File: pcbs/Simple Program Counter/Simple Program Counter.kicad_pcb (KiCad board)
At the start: 2 copper layers, 18 parts, among them U201 74HCT574, U202 74HC245, U203 74HC14

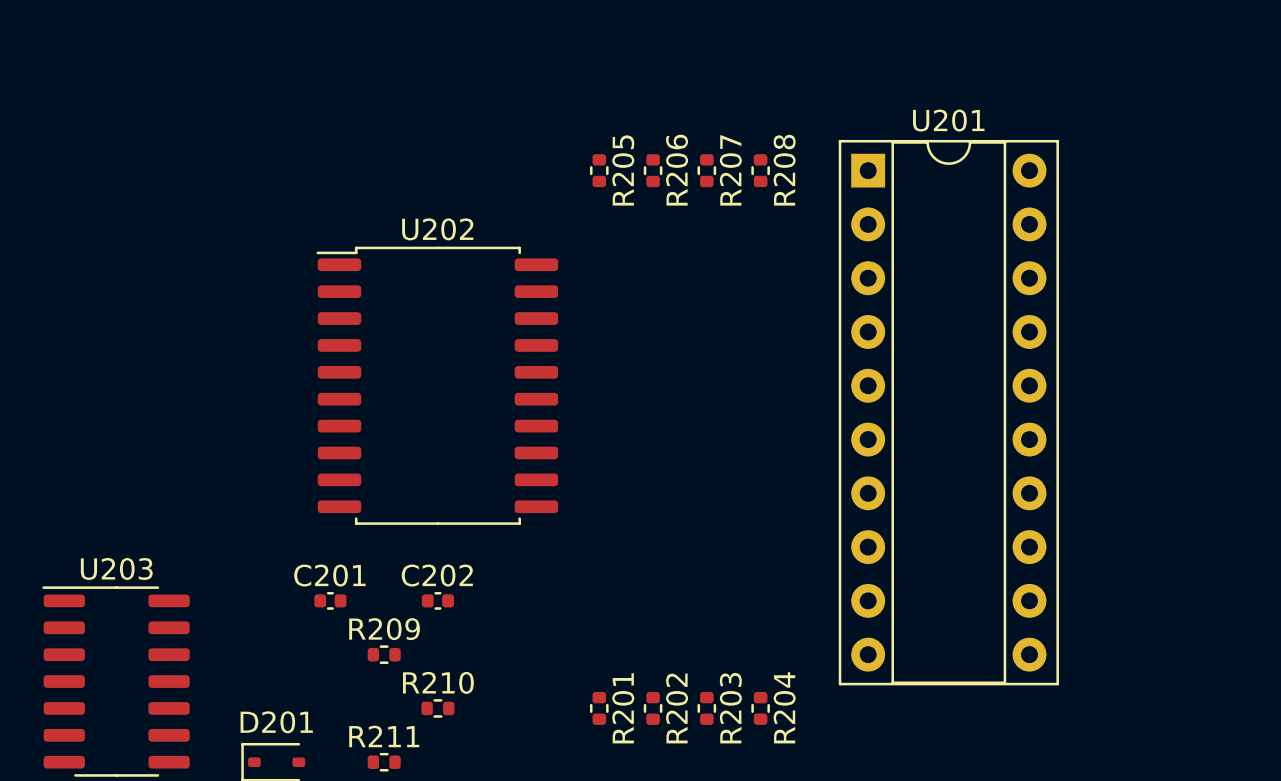
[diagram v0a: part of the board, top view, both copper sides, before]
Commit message: Adding indicator LEDs
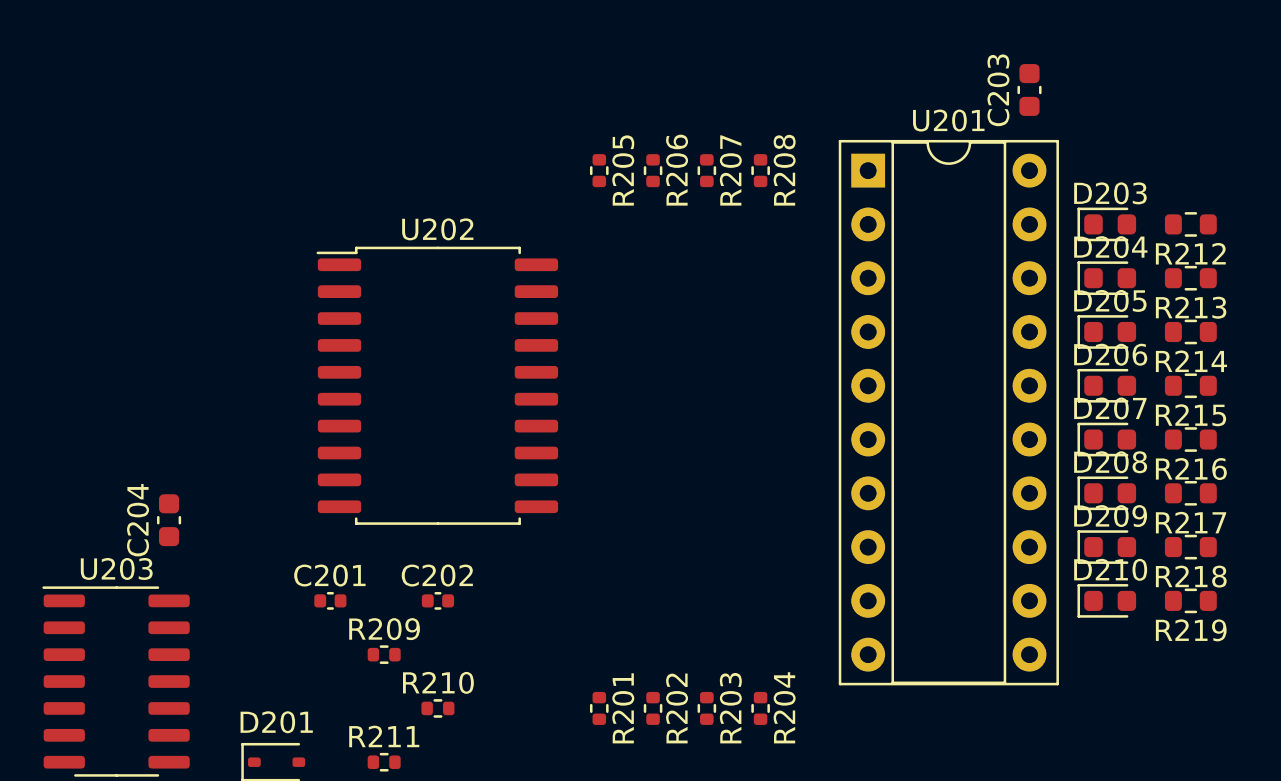
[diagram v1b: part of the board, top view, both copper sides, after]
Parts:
- added C203: 100n, Capacitor_SMD:C_0603_1608Metric, F.Cu at (139.7, 97.8)
- added C204: 100n, Capacitor_SMD:C_0603_1608Metric, F.Cu at (99.1, 118.1)
- added D203: GREEN, LED_SMD:LED_0603_1608Metric, F.Cu at (143.5, 104.1)
- added D204: GREEN, LED_SMD:LED_0603_1608Metric, F.Cu at (143.5, 106.7)
- added D205: GREEN, LED_SMD:LED_0603_1608Metric, F.Cu at (143.5, 109.2)
- added D206: GREEN, LED_SMD:LED_0603_1608Metric, F.Cu at (143.5, 111.8)
- added D207: GREEN, LED_SMD:LED_0603_1608Metric, F.Cu at (143.5, 114.3)
- added D208: GREEN, LED_SMD:LED_0603_1608Metric, F.Cu at (143.5, 116.8)
- added D209: GREEN, LED_SMD:LED_0603_1608Metric, F.Cu at (143.5, 119.4)
- added D210: GREEN, LED_SMD:LED_0603_1608Metric, F.Cu at (143.5, 121.9)
- added R212: 4k7, Resistor_SMD:R_0603_1608Metric, F.Cu at (147.3, 104.1)
- added R213: 4k7, Resistor_SMD:R_0603_1608Metric, F.Cu at (147.3, 106.7)
- added R214: 4k7, Resistor_SMD:R_0603_1608Metric, F.Cu at (147.3, 109.2)
- added R215: 4k7, Resistor_SMD:R_0603_1608Metric, F.Cu at (147.3, 111.8)
- added R216: 4k7, Resistor_SMD:R_0603_1608Metric, F.Cu at (147.3, 114.3)
- added R217: 4k7, Resistor_SMD:R_0603_1608Metric, F.Cu at (147.3, 116.8)
- added R218: 4k7, Resistor_SMD:R_0603_1608Metric, F.Cu at (147.3, 119.4)
- added R219: 4k7, Resistor_SMD:R_0603_1608Metric, F.Cu at (147.3, 121.9)
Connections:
- U201 pad 12: unconnected-(U201-Q7-Pad12) -> /PC/PC_{out}7
- U201 pad 13: unconnected-(U201-Q6-Pad13) -> /PC/PC_{out}6
- U201 pad 14: unconnected-(U201-Q5-Pad14) -> /PC/PC_{out}5
- U201 pad 15: unconnected-(U201-Q4-Pad15) -> /PC/PC_{out}4
- U201 pad 16: unconnected-(U201-Q3-Pad16) -> /PC/PC_{out}3
- U201 pad 17: unconnected-(U201-Q2-Pad17) -> /PC/PC_{out}2
- U201 pad 18: unconnected-(U201-Q1-Pad18) -> /PC/PC_{out}1
- U201 pad 19: unconnected-(U201-Q0-Pad19) -> /PC/PC_{out}0

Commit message: Thinking through some next bits
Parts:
- added D401: GREEN, LED_SMD:LED_0603_1608Metric, F.Cu at (62.2, 71.1)
- added D402: RED, LED_SMD:LED_0603_1608Metric, F.Cu at (62.2, 73.7)
- added D403: RED, LED_SMD:LED_0603_1608Metric, F.Cu at (62.2, 76.2)
- added D404: RED, LED_SMD:LED_0603_1608Metric, F.Cu at (62.2, 78.7)
- added D405: GREEN, LED_SMD:LED_0603_1608Metric, F.Cu at (62.2, 81.3)
- added D406: GREEN, LED_SMD:LED_0603_1608Metric, F.Cu at (62.2, 83.8)
- added D407: RED, LED_SMD:LED_0603_1608Metric, F.Cu at (62.2, 86.4)
- added D408: RED, LED_SMD:LED_0603_1608Metric, F.Cu at (62.2, 88.9)
- added D409: 1N4148WS, Diode_SMD:D_SOD-323, F.Cu at (91.2, 80.0)
- added D410: 1N4148WS, Diode_SMD:D_SOD-323, F.Cu at (91.2, 83.0)
- added D411: 1N4148WS, Diode_SMD:D_SOD-323, F.Cu at (91.2, 85.9)
- added R401: 4k7, Resistor_SMD:R_0603_1608Metric, F.Cu at (67.3, 71.1)
- added R402: 4k7, Resistor_SMD:R_0603_1608Metric, F.Cu at (67.3, 73.7)
- added R403: 4k7, Resistor_SMD:R_0603_1608Metric, F.Cu at (67.3, 76.2)
- added R404: 4k7, Resistor_SMD:R_0603_1608Metric, F.Cu at (67.3, 78.7)
- added R405: 4k7, Resistor_SMD:R_0603_1608Metric, F.Cu at (67.3, 81.3)
- added R406: 4k7, Resistor_SMD:R_0603_1608Metric, F.Cu at (67.3, 83.8)
- added R407: 4k7, Resistor_SMD:R_0603_1608Metric, F.Cu at (67.3, 86.4)
- added R408: 4k7, Resistor_SMD:R_0603_1608Metric, F.Cu at (67.3, 88.9)
- added R409: 200k, Resistor_SMD:R_0402_1005Metric, F.Cu at (94.8, 79.5)
- added U301: 74HC283, Package_DIP:DIP-16_W7.62mm_Socket, F.Cu at (108.0, 54.6)
- added U302: 74HC283, Package_DIP:DIP-16_W7.62mm_Socket, F.Cu at (123.2, 54.6)
- added U401: 74HC138, Package_DIP:DIP-16_W7.62mm_Socket, F.Cu at (48.3, 68.6)
- added U402: 74HC245, Package_SO:SOIC-20W_7.5x12.8mm_P1.27mm, F.Cu at (84.5, 66.7)
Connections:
- net /PC/PC_{out}0 renamed /Incrementer/PC_{curr}0
- net /PC/PC_{out}1 renamed /Incrementer/PC_{curr}1
- net /PC/PC_{out}2 renamed /Incrementer/PC_{curr}2
- net /PC/PC_{out}3 renamed /Incrementer/PC_{curr}3
- net /PC/PC_{out}4 renamed /Incrementer/PC_{curr}4
- net /PC/PC_{out}5 renamed /Incrementer/PC_{curr}5
- net /PC/PC_{out}6 renamed /Incrementer/PC_{curr}6
- net /PC/PC_{out}7 renamed /Incrementer/PC_{curr}7

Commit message: Getting close
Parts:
- added D501: 1N4148WS, Diode_SMD:D_SOD-323, F.Cu at (174.0, 52.1)
- added D502: 1N4148WS, Diode_SMD:D_SOD-323, F.Cu at (174.0, 54.6)
- added D503: 1N4148WS, Diode_SMD:D_SOD-323, F.Cu at (174.0, 57.1)
- added D504: 1N4148WS, Diode_SMD:D_SOD-323, F.Cu at (174.0, 59.7)
- added D505: 1N4148WS, Diode_SMD:D_SOD-323, F.Cu at (174.0, 62.2)
- added D506: 1N4148WS, Diode_SMD:D_SOD-323, F.Cu at (174.0, 64.8)
- added D507: 1N4148WS, Diode_SMD:D_SOD-323, F.Cu at (174.0, 67.3)
- added D508: 1N4148WS, Diode_SMD:D_SOD-323, F.Cu at (174.0, 69.8)
- added D509: GREEN, LED_SMD:LED_0603_1608Metric, F.Cu at (203.2, 111.8)
- added D510: GREEN, LED_SMD:LED_0603_1608Metric, F.Cu at (201.9, 94.0)
- added R501: 200k, Resistor_SMD:R_0402_1005Metric, F.Cu at (160.0, 53.3)
- added R502: 200k, Resistor_SMD:R_0402_1005Metric, F.Cu at (162.6, 53.3)
- added R503: 200k, Resistor_SMD:R_0402_1005Metric, F.Cu at (165.1, 53.3)
- added R504: 200k, Resistor_SMD:R_0402_1005Metric, F.Cu at (167.6, 53.3)
- added R505: 200k, Resistor_SMD:R_0402_1005Metric, F.Cu at (160.0, 69.8)
- added R506: 200k, Resistor_SMD:R_0402_1005Metric, F.Cu at (162.6, 69.8)
- added R507: 200k, Resistor_SMD:R_0402_1005Metric, F.Cu at (165.1, 69.8)
- added R508: 200k, Resistor_SMD:R_0402_1005Metric, F.Cu at (167.6, 69.8)
- added R509: 200k, Resistor_SMD:R_0402_1005Metric, F.Cu at (183.6, 67.3)
- added R510: 4k7, Resistor_SMD:R_0603_1608Metric, F.Cu at (198.1, 111.8)
- added R511: 4k7, Resistor_SMD:R_0603_1608Metric, F.Cu at (198.1, 94.0)
- added U101: 74HC00, Package_DIP:DIP-14_W7.62mm_Socket, F.Cu at (52.9, 131.5)
- added U102: 74HC245, Package_SO:SOIC-20W_7.5x12.8mm_P1.27mm, F.Cu at (69.0, 136.5)
- added U501: 74HC245, Package_SO:SOIC-20W_7.5x12.8mm_P1.27mm, F.Cu at (188.0, 99.1)
- added U502: 74HC245, Package_SO:SOIC-20W_7.5x12.8mm_P1.27mm, F.Cu at (188.0, 115.6)
- added U503: 74HC245, Package_SO:SOIC-20W_7.5x12.8mm_P1.27mm, F.Cu at (152.4, 61.0)
- added U504: 74HC14, Package_SO:SOIC-14_3.9x8.7mm_P1.27mm, F.Cu at (184.2, 57.1)
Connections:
- net /Instructions/C0 renamed /C0
- net /Instructions/C1 renamed /C1
- net /Instructions/C2 renamed /C2
- net /Instructions/C3 renamed /C3
- net /Instructions/C4 renamed /C4
- net /Instructions/C5 renamed /C5
- net /Instructions/C6 renamed /C6
- net /Instructions/C7 renamed /C7
- net /Instructions/Commit renamed /Commit
- net /Instructions/Execute renamed /Execute
- net /Instructions/PC_{Update} renamed /PC_{Update}
- net /Instructions/~{Active} renamed /~{Active}
- U202 pad 2: /PC/PC_{in}0 -> /Instructions/PC_{next}0
- U202 pad 3: /PC/PC_{in}1 -> /Instructions/PC_{next}1
- U202 pad 4: /PC/PC_{in}2 -> /Instructions/PC_{next}2
- U202 pad 5: /PC/PC_{in}3 -> /Instructions/PC_{next}3
- U202 pad 6: /PC/PC_{in}4 -> /Instructions/PC_{next}4
- U202 pad 7: /PC/PC_{in}5 -> /Instructions/PC_{next}5
- U202 pad 8: /PC/PC_{in}6 -> /Instructions/PC_{next}6
- U202 pad 9: /PC/PC_{in}7 -> /Instructions/PC_{next}7
- U301 pad 1: /Incrementer/PC_{next}1 -> /Incrementer/PC_{inc}1
- U301 pad 10: /Incrementer/PC_{next}3 -> /Incrementer/PC_{inc}3
- U301 pad 13: /Incrementer/PC_{next}2 -> /Incrementer/PC_{inc}2
- U301 pad 4: /Incrementer/PC_{next}0 -> /Incrementer/PC_{inc}0
- U301 pad 6: /Incrementer/~{HALT} -> /Instructions/~{Decoded}0
- U302 pad 1: /Incrementer/PC_{next}5 -> /Incrementer/PC_{inc}5
- U302 pad 10: /Incrementer/PC_{next}7 -> /Incrementer/PC_{inc}7
- U302 pad 13: /Incrementer/PC_{next}6 -> /Incrementer/PC_{inc}6
- U302 pad 4: /Incrementer/PC_{next}4 -> /Incrementer/PC_{inc}4
- U402 pad 2: /Instructions/PC_{curr}0 -> /Incrementer/PC_{curr}0
- U402 pad 3: /Instructions/PC_{curr}1 -> /Incrementer/PC_{curr}1
- U402 pad 4: /Instructions/PC_{curr}2 -> /Incrementer/PC_{curr}2
- U402 pad 5: /Instructions/PC_{curr}3 -> /Incrementer/PC_{curr}3
- U402 pad 6: /Instructions/PC_{curr}4 -> /Incrementer/PC_{curr}4
- U402 pad 7: /Instructions/PC_{curr}5 -> /Incrementer/PC_{curr}5
- U402 pad 8: /Instructions/PC_{curr}6 -> /Incrementer/PC_{curr}6
- U402 pad 9: /Instructions/PC_{curr}7 -> /Incrementer/PC_{curr}7

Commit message: Doing a (very) little routing
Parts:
- moved U502 23.9 mm to (164.3, 118.7)
- moved D510 23.9 mm to (178.3, 97.2)
- moved R510 23.9 mm to (174.5, 114.9)
- moved R511 23.9 mm to (174.5, 97.2)
- moved U501 23.9 mm to (164.3, 102.2)
- moved D509 23.9 mm to (179.6, 114.9)
- moved R205 10.5 mm to (129.5, 99.1)
- moved R201 10.2 mm to (129.5, 127.0)
- moved R206 6.84 mm to (128.3, 99.1)
- moved R202 6.35 mm to (128.3, 127.0)
- moved U202 6.35 mm to (118.1, 111.8)
- moved R207 3.59 mm to (127.0, 99.1)
- moved R208 2.84 mm to (125.7, 99.1)
- moved R203 2.54 mm to (127.0, 127.0)
- moved R204 1.27 mm to (125.7, 127.0)
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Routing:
- net Net-(U201-D3): track 0.00 -> 21.8 mm, vias 0 -> 1
- net Net-(U201-D4): track 0.00 -> 21.8 mm, vias 0 -> 1
- net Net-(U201-D2): track 0.00 -> 20.5 mm, vias 0 -> 1
- net Net-(U201-D5): track 0.00 -> 20.5 mm, vias 0 -> 1
- net Net-(U201-D1): track 0.00 -> 19.2 mm, vias 0 -> 1
- net Net-(U201-D6): track 0.00 -> 19.2 mm, vias 0 -> 1
- net Net-(U201-D0): track 0.00 -> 18.0 mm, vias 0 -> 1
- net Net-(U201-D7): track 0.00 -> 18.0 mm, vias 0 -> 1
